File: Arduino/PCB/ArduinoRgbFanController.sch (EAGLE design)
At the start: 60 parts, among them IC2 ARDUINO_MKRFOX1200PROTOPADS, Q1 IRLML930, Q2 2N7002, Q3 2N7002, Q4 IRLML930

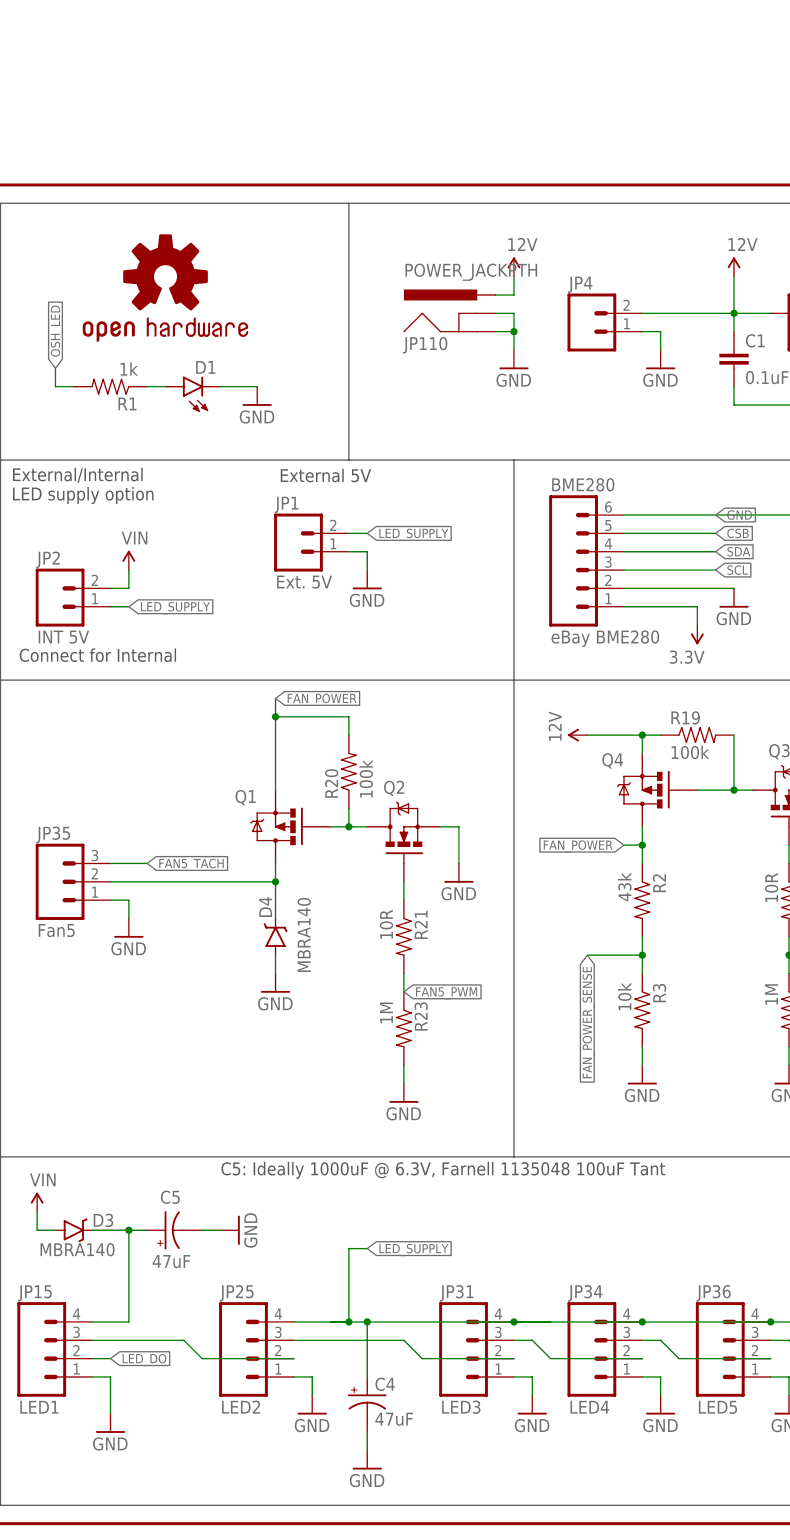
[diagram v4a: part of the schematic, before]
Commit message: Added required external capacitor and part values.
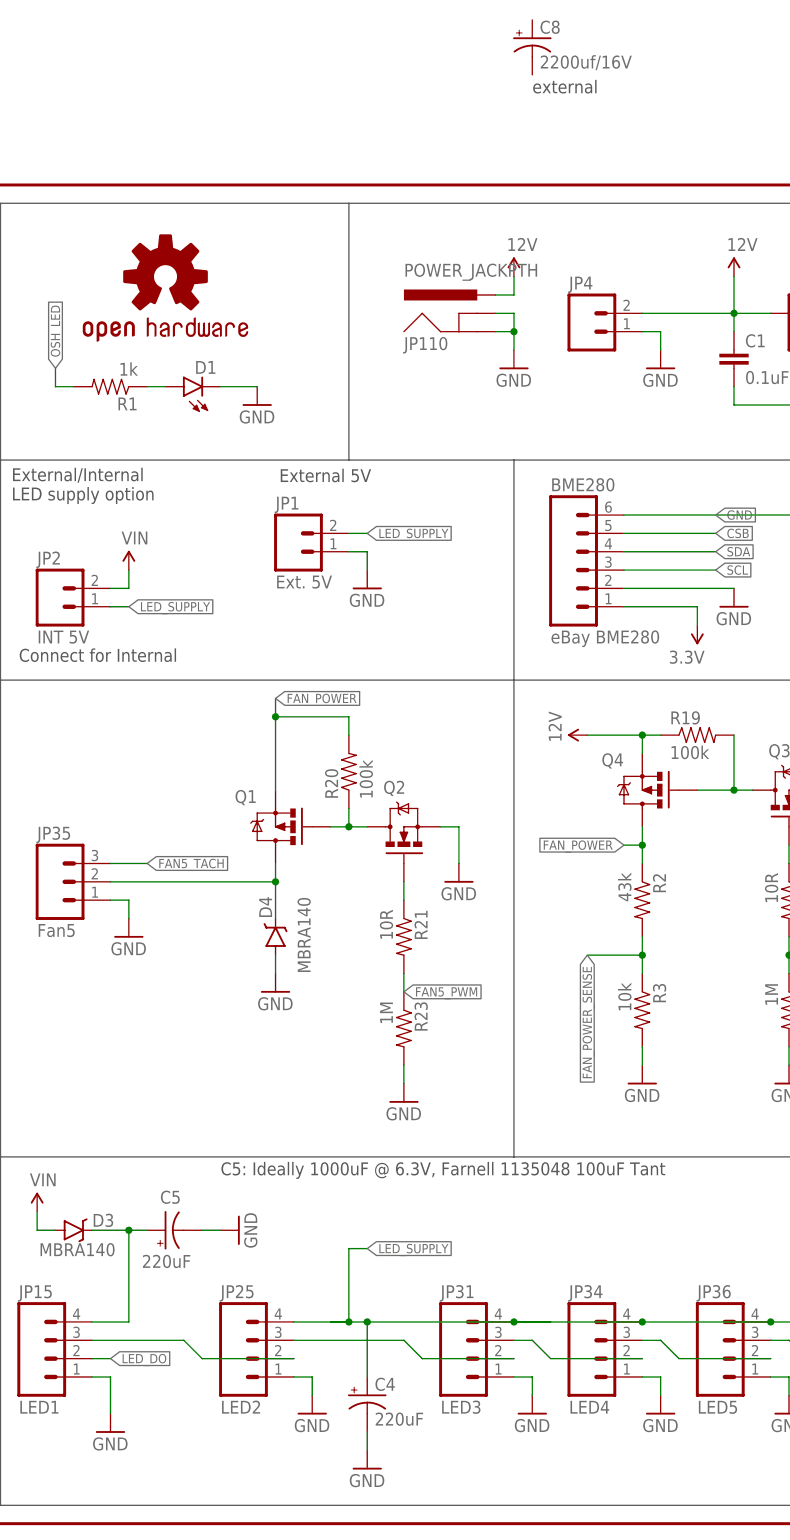
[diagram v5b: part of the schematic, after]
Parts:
- added C8: 2200uf/16V, SparkFun-Capacitors:1000UF-25V(PTH)KIT
- C4: value 47uF -> 220uF; FARNELL (none) -> 2491486
- C5: value 47uF -> 220uF; FARNELL 1135048 -> 2491486
- JP15, JP25, JP31, JP34, JP36, JP37: FARNELL (none) -> 2063775
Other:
- note added: "external"
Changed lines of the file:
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@@
 <part name="JP13" library="SparkFun-Connectors" deviceset="M04" device="POLAR" value="Fan4"/>
 <part name="GND5" library="SparkFun-Aesthetics" deviceset="GND" device=""/>
-<part name="JP15" library="SparkFun-Connectors" deviceset="M04" device="PTH" value="LED1"/>
-<part name="JP25" library="SparkFun-Connectors" deviceset="M04" device="PTH" value="LED2"/>
-<part name="JP31" library="SparkFun-Connectors" deviceset="M04" device="PTH" value="LED3"/>
-<part name="JP34" library="SparkFun-Connectors" deviceset="M04" device="PTH" value="LED4"/>
+<part name="JP15" library="SparkFun-Connectors" deviceset="M04" device="PTH" value="LED1">
+<attribute name="FARNELL" value="2063775"/>
+</part>
+<part name="JP25" library="SparkFun-Connectors" deviceset="M04" device="PTH" value="LED2">
+<attribute name="FARNELL" value="2063775"/>
+</part>
+<part name="JP31" library="SparkFun-Connectors" deviceset="M04" device="PTH" value="LED3">
+<attribute name="FARNELL" value="2063775"/>
+</part>
+<part name="JP34" library="SparkFun-Connectors" deviceset="M04" device="PTH" value="LED4">
+<attribute name="FARNELL" value="2063775"/>
+</part>
 <part name="GND17" library="SparkFun-Aesthetics" deviceset="GND" device=""/>
 <part name="GND18" library="SparkFun-Aesthetics" deviceset="GND" device=""/>
@@
 <part name="GND20" library="SparkFun-Aesthetics" deviceset="GND" device=""/>
 <part name="JP35" library="SparkFun-Connectors" deviceset="M03" device="POLAR" value="Fan5"/>
-<part name="JP36" library="SparkFun-Connectors" deviceset="M04" device="PTH" value="LED5"/>
-<part name="JP37" library="SparkFun-Connectors" deviceset="M04" device="PTH" value="LED6"/>
+<part name="JP36" library="SparkFun-Connectors" deviceset="M04" device="PTH" value="LED5">
+<attribute name="FARNELL" value="2063775"/>
+</part>
+<part name="JP37" library="SparkFun-Connectors" deviceset="M04" device="PTH" value="LED6">
+<attribute name="FARNELL" value="2063775"/>
+</part>
 <part name="GND21" library="SparkFun-Aesthetics" deviceset="GND" device=""/>
 <part name="GND22" library="SparkFun-Aesthetics" deviceset="GND" device=""/>
@@
 <part name="SUPPLY10" library="SparkFun-Aesthetics" deviceset="VIN" device=""/>
 <part name="R11" library="SparkFun-Resistors" deviceset="RESISTOR" device="0805-RES" value="470R"/>
-<part name="C4" library="SparkFun-Capacitors" deviceset="47UF-10V-10%(TANT)" device="" value="47uF"/>
-<part name="C5" library="SparkFun-Capacitors" deviceset="47UF-10V-10%(TANT)" device="" value="47uF">
-<attribute name="FARNELL" value="1135048"/>
+<part name="C4" library="SparkFun-Capacitors" deviceset="47UF-10V-10%(TANT)" device="" value="220uF">
+<attribute name="FARNELL" value="2491486"/>
+</part>
+<part name="C5" library="SparkFun-Capacitors" deviceset="47UF-10V-10%(TANT)" device="" value="220uF">
+<attribute name="FARNELL" value="2491486"/>
 </part>
 <part name="GND10" library="SparkFun-Aesthetics" deviceset="GND" device=""/>
@@
 <part name="R3" library="SparkFun-Resistors" deviceset="RESISTOR" device="0805-RES" value="10k"/>
 <part name="GND7" library="SparkFun-Aesthetics" deviceset="GND" device=""/>
+<part name="C8" library="SparkFun-Capacitors" deviceset="1000UF-25V(PTH)" device="KIT" value="2200uf/16V"/>
 </parts>
 <sheets>
@@
 * Can Fans 1 &amp; 2, 3 &amp; 4 share pwm signals?</text>
 <text x="33.02" y="48.26" size="1.778" layer="97">C5: Ideally 1000uF @ 6.3V, Farnell 1135048 100uF Tant</text>
+<text x="76.2" y="198.12" size="1.778" layer="97">external</text>
 </plain>
 <instances>
@@
 <instance part="JP13" gate="G$1" x="223.52" y="76.2"/>
 <instance part="GND5" gate="1" x="147.32" y="68.58"/>
-<instance part="JP15" gate="G$1" x="10.16" y="22.86"/>
-<instance part="JP25" gate="G$1" x="38.1" y="22.86"/>
-<instance part="JP31" gate="G$1" x="68.58" y="22.86"/>
-<instance part="JP34" gate="G$1" x="86.36" y="22.86"/>
+<instance part="JP15" gate="G$1" x="10.16" y="22.86">
+<attribute name="FARNELL" x="10.16" y="22.86" size="1.778" layer="96" display="off"/>
+</instance>
+<instance part="JP25" gate="G$1" x="38.1" y="22.86">
+<attribute name="FARNELL" x="38.1" y="22.86" size="1.778" layer="96" display="off"/>
+</instance>
+<instance part="JP31" gate="G$1" x="68.58" y="22.86">
+<attribute name="FARNELL" x="68.58" y="22.86" size="1.778" layer="96" display="off"/>
+</instance>
+<instance part="JP34" gate="G$1" x="86.36" y="22.86">
+<attribute name="FARNELL" x="86.36" y="22.86" size="1.778" layer="96" display="off"/>
+</instance>
 <instance part="GND17" gate="1" x="17.78" y="12.7"/>
 <instance part="GND18" gate="1" x="45.72" y="15.24"/>
@@
 <instance part="GND20" gate="1" x="93.98" y="15.24"/>
 <instance part="JP35" gate="G$1" x="10.16" y="88.9"/>
-<instance part="JP36" gate="G$1" x="104.14" y="22.86"/>
-<instance part="JP37" gate="G$1" x="121.92" y="22.86"/>
+<instance part="JP36" gate="G$1" x="104.14" y="22.86">
+<attribute name="FARNELL" x="104.14" y="22.86" size="1.778" layer="96" display="off"/>
+</instance>
+<instance part="JP37" gate="G$1" x="121.92" y="22.86">
+<attribute name="FARNELL" x="121.92" y="22.86" size="1.778" layer="96" display="off"/>
+</instance>
 <instance part="GND21" gate="1" x="111.76" y="15.24"/>
 <instance part="GND22" gate="1" x="129.54" y="15.24"/>
@@
 <attribute name="VALUE" x="173.99" y="164.338" size="1.778" layer="96"/>
 </instance>
-<instance part="C4" gate="G$1" x="53.34" y="17.78"/>
+<instance part="C4" gate="G$1" x="53.34" y="17.78">
+<attribute name="FARNELL" x="53.34" y="17.78" size="1.778" layer="96" display="off"/>
+</instance>
 <instance part="C5" gate="G$1" x="25.4" y="40.64" smashed="yes" rot="R90">
 <attribute name="NAME" x="24.638" y="44.323" size="1.778" layer="95"/>
@@
 </instance>
 <instance part="GND7" gate="1" x="91.44" y="60.96"/>
+<instance part="C8" gate="G$1" x="76.2" y="205.74"/>
 </instances>
 <busses>
